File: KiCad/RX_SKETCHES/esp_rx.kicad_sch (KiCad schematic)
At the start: 5 parts, among them U2 ESP32-WROOM-32U

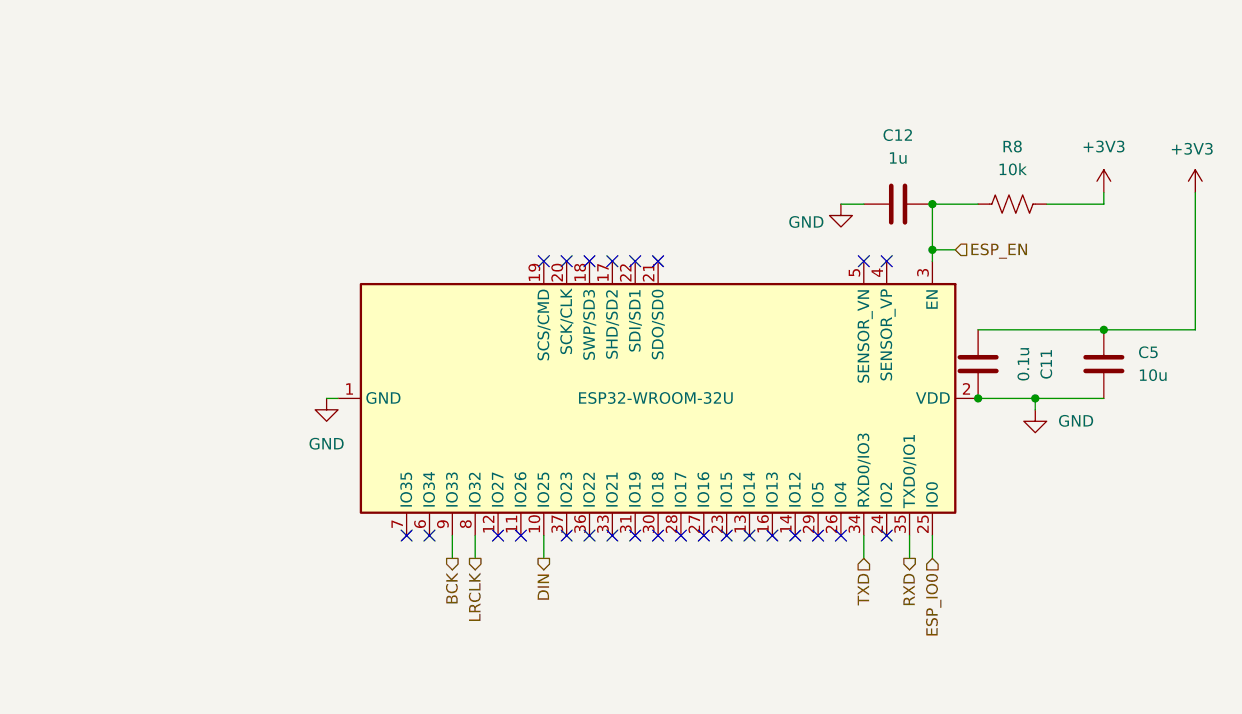
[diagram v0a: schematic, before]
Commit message: Rewire RX hierarchical labels and mark proto DNP parts.
Keep the rotated WROOM-32U and breadboard I2S GPIOs, but attach
ESP_EN/IO0, UART, and BCK/DIN/LRCLK to the pins that actually sit
there after the 270° rotate. Move PCM5102 I2S off FMT/DEMP/XSMT,
put amp shutdown on ~{SHDN}, keep the datasheet 470R+2.2nF filter,
DNP the experimental pot pad and MAX97220A input resistors, and
switch schematic passives to 0805 for hand assembly.

Co-authored-by: luciano <dlmuschamp@users.noreply.github.com>
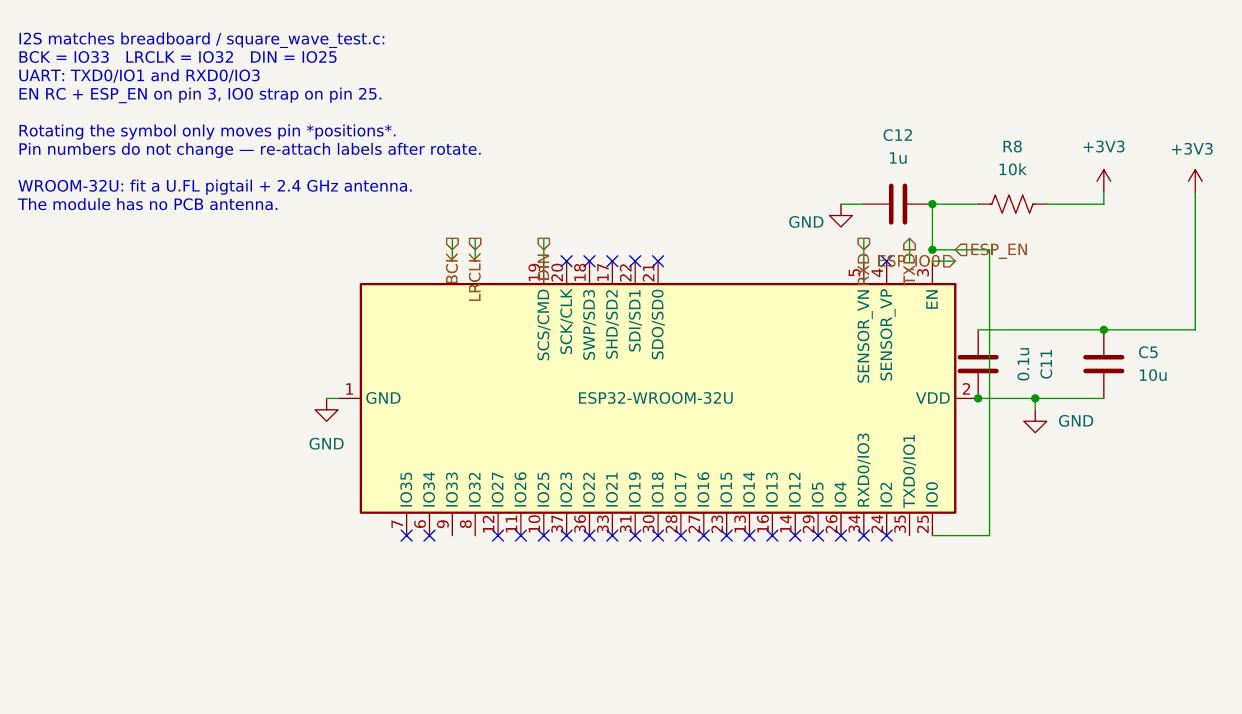
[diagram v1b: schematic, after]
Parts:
- C11, C12, C5: footprint Capacitor_SMD:C_0201_0603Metric -> Capacitor_SMD:C_0805_2012Metric
- R8: footprint Resistor_SMD:R_0201_0603Metric -> Resistor_SMD:R_0805_2012Metric
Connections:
- net BCK: no longer U2.9 (IO33)
- net DIN: now also U2.19 (SCS/CMD); no longer U2.10 (IO25)
- net ESP_EN: now also U2.25 (IO0); no longer U2.3 (EN)
- net ESP_IO0: now also U2.3 (EN); no longer U2.25 (IO0)
- net LRCLK: no longer U2.8 (IO32)
- net RXD: now also U2.5 (SENSOR_VN); no longer U2.35 (TXD0/IO1)
- net TXD: no longer U2.34 (RXD0/IO3)
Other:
- note added: "I2S matches breadboard / square_wave_test.c: BCK = IO33 LRCLK = IO32 DIN = IO25 UART: TXD0/IO1 and RXD0/IO3 EN RC + ESP_EN on pin 3, IO0 strap on pin 25. Rotating the symbol only moves pin *positions*. Pin numbers do not change — re-attach labels after rotate. WROOM-32U: fit a U.FL pigtail + 2.4 GHz antenna. The module has no PCB antenna."
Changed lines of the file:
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@@
 		(comment 3 "Will enter boot mode when communicating over UART. Functions normally otherwise.")
+	)
+	(text "I2S matches breadboard / square_wave_test.c:\nBCK = IO33   LRCLK = IO32   DIN = IO25\nUART: TXD0/IO1 and RXD0/IO3\nEN RC + ESP_EN on pin 3, IO0 strap on pin 25.\n\nRotating the symbol only moves pin *positions*.\nPin numbers do not change — re-attach labels after rotate.\n\nWROOM-32U: fit a U.FL pigtail + 2.4 GHz antenna.\nThe module has no PCB antenna."
+		(exclude_from_sim no)
+		(at 24.13 27.94 0)
+		(effects
+			(font
+				(size 1.27 1.27)
+			)
+			(justify left)
+		)
 	)
 	(junction
@@
 	)
 	(no_connect
-		(at 118.11 43.18)
+		(at 118.11 73.66)
 	)
 	(no_connect
@@
 	)
 	(no_connect
-		(at 82.55 43.18)
+		(at 82.55 73.66)
 	)
 	(no_connect
@@
 	(wire
 		(pts
-			(xy 118.11 73.66) (xy 118.11 76.2)
+			(xy 123.19 43.18) (xy 123.19 40.64)
 		)
 		(stroke
@@
 	(wire
 		(pts
-			(xy 72.39 73.66) (xy 72.39 76.2)
-		)
-		(stroke
-			(width 0)
-			(type default)
-		)
-	)
-	(wire
-		(pts
-			(xy 123.19 73.66) (xy 123.19 76.2)
+			(xy 72.39 43.18) (xy 72.39 40.64)
+		)
+		(stroke
+			(width 0)
+			(type default)
+		)
+	)
+	(wire
+		(pts
+			(xy 118.11 43.18) (xy 118.11 40.64)
 		)
 		(stroke
@@
 	(wire
 		(pts
-			(xy 74.93 76.2) (xy 74.93 73.66)
+			(xy 74.93 43.18) (xy 74.93 40.64)
 		)
 		(stroke
@@
 	(wire
 		(pts
-			(xy 82.55 73.66) (xy 82.55 76.2)
-		)
-		(stroke
-			(width 0)
-			(type default)
-		)
-	)
-	(wire
-		(pts
-			(xy 125.73 43.18) (xy 125.73 41.91)
+			(xy 82.55 43.18) (xy 82.55 40.64)
+		)
+		(stroke
+			(width 0)
+			(type default)
+		)
+	)
+	(wire
+		(pts
+			(xy 125.73 73.66) (xy 132.08 73.66)
+		)
+		(stroke
+			(width 0)
+			(type default)
+		)
+	)
+	(wire
+		(pts
+			(xy 132.08 73.66) (xy 132.08 41.91)
+		)
+		(stroke
+			(width 0)
+			(type default)
+		)
+	)
+	(wire
+		(pts
+			(xy 132.08 41.91) (xy 128.27 41.91)
 		)
 		(stroke
@@
 	(wire
 		(pts
-			(xy 125.73 73.66) (xy 125.73 76.2)
+			(xy 125.73 43.18) (xy 128.27 43.18)
 		)
 		(stroke
@@
 	(hierarchical_label "RXD"
 		(shape output)
-		(at 123.19 76.2 270)
+		(at 118.11 40.64 90)
 		(effects
 			(font
@@
 	(hierarchical_label "ESP_IO0"
 		(shape input)
-		(at 125.73 76.2 270)
+		(at 128.27 43.18 0)
 		(effects
 			(font
@@
 	(hierarchical_label "LRCLK"
 		(shape output)
-		(at 74.93 76.2 270)
+		(at 74.93 40.64 90)
 		(effects
 			(font
@@
 	(hierarchical_label "BCK"
 		(shape output)
-		(at 72.39 76.2 270)
+		(at 72.39 40.64 90)
 		(effects
 			(font
@@
 	(hierarchical_label "DIN"
 		(shape output)
-		(at 82.55 76.2 270)
+		(at 82.55 40.64 90)
 		(effects
 			(font
@@
 	(hierarchical_label "TXD"
 		(shape input)
-		(at 118.11 76.2 270)
+		(at 123.19 40.64 90)
 		(effects
 			(font
@@
 			)
 		)
-		(property "Footprint" "Capacitor_SMD:C_0201_0603Metric"
+		(property "Footprint" "Capacitor_SMD:C_0805_2012Metric"
 			(at 145.7452 58.42 0)
 			(hide yes)
@@
 			)
 		)
-		(property "Footprint" "Resistor_SMD:R_0201_0603Metric"
+		(property "Footprint" "Resistor_SMD:R_0805_2012Metric"
 			(at 134.366 37.846 90)
 			(hide yes)
@@
 			)
 		)
-		(property "Footprint" "Capacitor_SMD:C_0201_0603Metric"
+		(property "Footprint" "Capacitor_SMD:C_0805_2012Metric"
 			(at 125.73 35.8648 0)
 			(hide yes)
@@
 			)
 		)
-		(property "Footprint" "Capacitor_SMD:C_0201_0603Metric"
+		(property "Footprint" "Capacitor_SMD:C_0805_2012Metric"
 			(at 131.7752 58.42 0)
 			(hide yes)

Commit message: Document the RX transfer and add ANT1 on the ESP sheet.
Rewrite the README for no display, matching 10,000 mAh USB-C banks
on TX and RX, the firmware I2S map, and first-board KiCad pitfalls.
Place ANT1 as a BOM-only 2.4 GHz U.FL pigtail that mates to the
WROOM-32U module connector (no GPIO, no PCB antenna footprint).

Co-authored-by: luciano <dlmuschamp@users.noreply.github.com>
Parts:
- added ANT1: 2.4GHz_U.FL_pigtail, symbol Device:Antenna
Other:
- note added: "I2S matches breadboard / square_wave_test.c: BCK = IO33 LRCLK = IO32 DIN = IO25 UART: TXD0/IO1 and RXD0/IO3 EN RC + ESP_EN on pin 3, IO0 strap on pin 25. Rotating the symbol only moves pin *positions*. Pin numbers do not change — re-attach labels after rotate. ANT1 = 2.4 GHz U.FL/IPEX pigtail (BOM only). Mates to the 32U on-module U.FL. No GPIO, no PCB antenna."
- note removed: "I2S matches breadboard / square_wave_test.c: BCK = IO33 LRCLK = IO32 DIN = IO25 UART: TXD0/IO1 and RXD0/IO3 EN RC + ESP_EN on pin 3, IO0 strap on pin 25. Rotating the symbol only moves pin *positions*. Pin numbers do not change — re-attach labels after rotate. WROOM-32U: fit a U.FL pigtail + 2.4 GHz antenna. The module has no PCB antenna."
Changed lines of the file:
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@@
 		(comment 3 "Will enter boot mode when communicating over UART. Functions normally otherwise.")
 	)
-	(text "I2S matches breadboard / square_wave_test.c:\nBCK = IO33   LRCLK = IO32   DIN = IO25\nUART: TXD0/IO1 and RXD0/IO3\nEN RC + ESP_EN on pin 3, IO0 strap on pin 25.\n\nRotating the symbol only moves pin *positions*.\nPin numbers do not change — re-attach labels after rotate.\n\nWROOM-32U: fit a U.FL pigtail + 2.4 GHz antenna.\nThe module has no PCB antenna."
+	(text "I2S matches breadboard / square_wave_test.c:\nBCK = IO33   LRCLK = IO32   DIN = IO25\nUART: TXD0/IO1 and RXD0/IO3\nEN RC + ESP_EN on pin 3, IO0 strap on pin 25.\n\nRotating the symbol only moves pin *positions*.\nPin numbers do not change — re-attach labels after rotate.\n\nANT1 = 2.4 GHz U.FL/IPEX pigtail (BOM only).\nMates to the 32U on-module U.FL. No GPIO, no PCB antenna."
 		(exclude_from_sim no)
 		(at 24.13 27.94 0)
@@
 					(unit 1)
 				)
+			)
+		)
+	)
+	(symbol
+		(lib_id "Device:Antenna")
+		(at 36.83 88.9 0)
+		(unit 1)
+		(body_style 1)
+		(exclude_from_sim yes)
+		(in_bom yes)
+		(on_board no)
+		(in_pos_files no)
+		(dnp no)
+		(property "Reference" "ANT1"
+			(at 36.83 82.55 0)
+			(show_name no)
+			(do_not_autoplace no)
+			(effects
+				(font
+					(size 1.27 1.27)
+				)
+			)
+		)
+		(property "Value" "2.4GHz_U.FL_pigtail"
+			(at 41.91 88.9 0)
+			(show_name no)
+			(do_not_autoplace no)
+			(effects
+				(font
+					(size 1.27 1.27)
+				)
+				(justify left)
+			)
+		)
+		(property "Footprint" ""
+			(at 36.83 88.9 0)
+			(hide yes)
+			(show_name no)
+			(do_not_autoplace no)
+			(effects
+				(font
+					(size 1.27 1.27)
+				)
+			)
+		)
+		(property "Datasheet" ""
+			(at 36.83 88.9 0)
+			(hide yes)
+			(show_name no)
+			(do_not_autoplace no)
+			(effects
+				(font
+					(size 1.27 1.27)
+				)
+			)
+		)
+		(property "Description" "2.4 GHz 50 ohm antenna on U.FL/IPEX pigtail. Mates to WROOM-32U module U.FL. Not a GPIO."
+			(at 36.83 88.9 0)
+			(hide yes)
+			(show_name no)
+			(do_not_autoplace no)
+			(effects
+				(font
+					(size 1.27 1.27)
+				)
+			)
+		)
+		(instances
+			(project "ESP_32_IEM_RIG_RX_VER_1.0"
+				(path "/98787dcf-424f-4647-bb79-9127f0f74bda/12633c0c-fb68-4c25-af81-bead6c15ab98"
+					(reference "ANT1")
+					(unit 1)
+				)

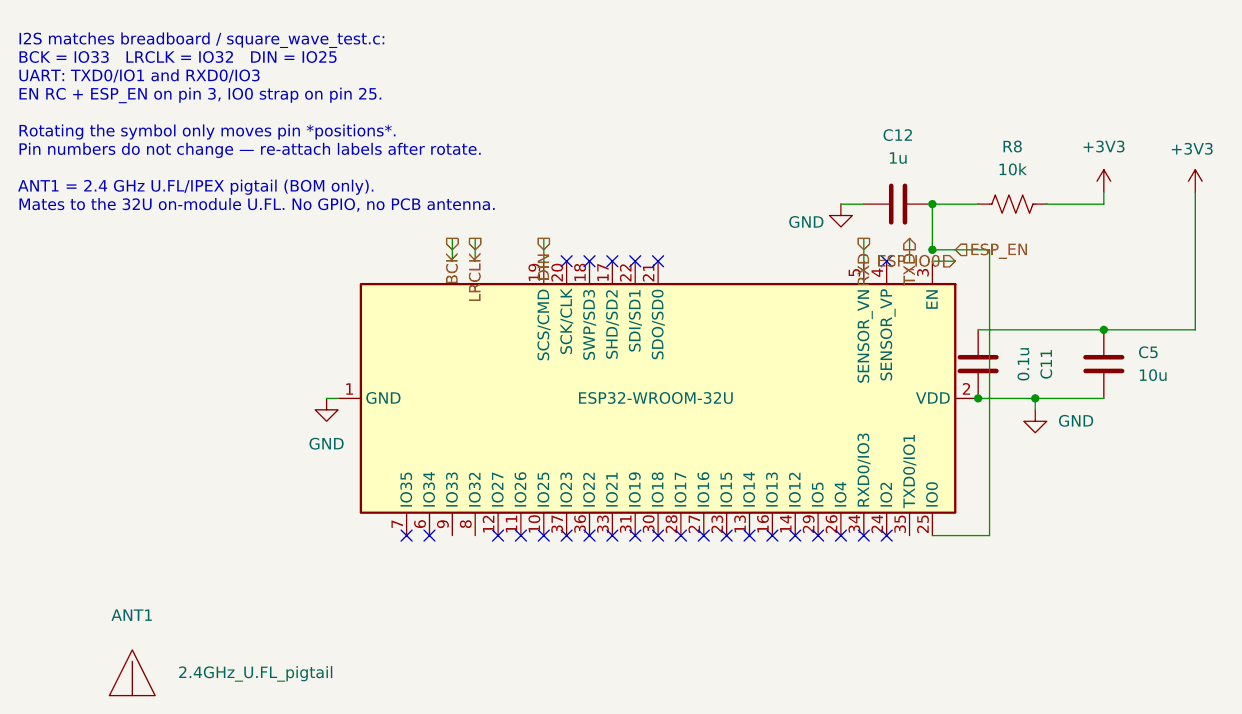
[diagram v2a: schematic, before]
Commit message: Align RX passives and analog nets with the part datasheets.
Put every R/C on the 0805 HandSolder footprint. Rewire the PCM5102
470R filter onto OUTL/OUTR, decouple LDOO, and land the flying cap
on CAPP/CAPM. Move the headphone jack off PVSS/SVSS onto OUTL/OUTR
with a PVSS hold cap. Tie CP2102C VIO to VDD, pull RST up, add the
LM3940 0.47uF Cin, and pull IO0 up for normal boot.

Co-authored-by: luciano <dlmuschamp@users.noreply.github.com>
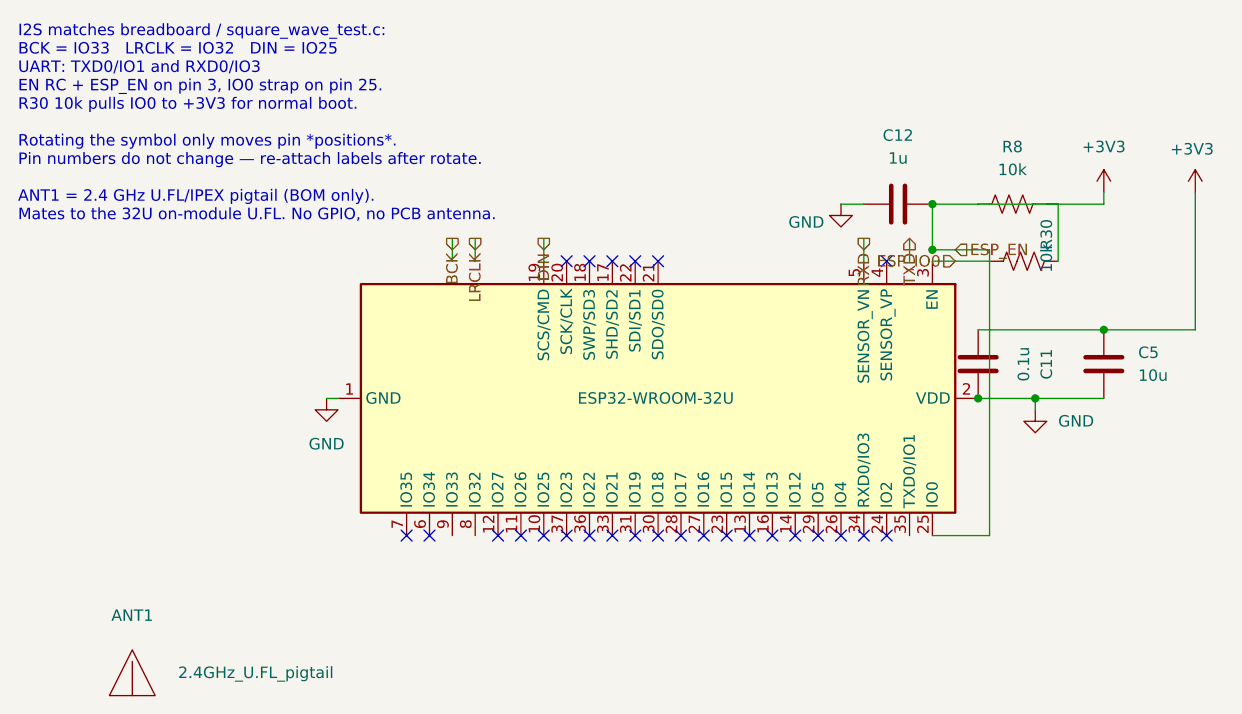
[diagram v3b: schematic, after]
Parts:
- added R30: 10k, Resistor_SMD:R_0805_2012Metric_Pad1.20x1.40mm_HandSolder, symbol Device:R_US
- C11, C12, C5: footprint Capacitor_SMD:C_0805_2012Metric -> Capacitor_SMD:C_0805_2012Metric_Pad1.15x1.40mm_HandSolder
- R8: footprint Resistor_SMD:R_0805_2012Metric -> Resistor_SMD:R_0805_2012Metric_Pad1.20x1.40mm_HandSolder
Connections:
- net ESP_EN is gone; now on net +3V3: C12.2, R8.2, U2.25 (IO0)
- net +3V3: now also R30.2
- net ESP_IO0: now also R30.1
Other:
- note added: "I2S matches breadboard / square_wave_test.c: BCK = IO33 LRCLK = IO32 DIN = IO25 UART: TXD0/IO1 and RXD0/IO3 EN RC + ESP_EN on pin 3, IO0 strap on pin 25. R30 10k pulls IO0 to +3V3 for normal boot. Rotating the symbol only moves pin *positions*. Pin numbers do not change — re-attach labels after rotate. ANT1 = 2.4 GHz U.FL/IPEX pigtail (BOM only). Mates to the 32U on-module U.FL. No GPIO, no PCB a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"
- note removed: "I2S matches breadboard / square_wave_test.c: BCK = IO33 LRCLK = IO32 DIN = IO25 UART: TXD0/IO1 and RXD0/IO3 EN RC + ESP_EN on pin 3, IO0 strap on pin 25. Rotating the symbol only moves pin *positions*. Pin numbers do not change — re-attach labels after rotate. ANT1 = 2.4 GHz U.FL/IPEX pigtail (BOM only). Mates to the 32U on-module U.FL. No GPIO, no PCB antenna."
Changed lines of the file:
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@@
 		(comment 3 "Will enter boot mode when communicating over UART. Functions normally otherwise.")
 	)
-	(text "I2S matches breadboard / square_wave_test.c:\nBCK = IO33   LRCLK = IO32   DIN = IO25\nUART: TXD0/IO1 and RXD0/IO3\nEN RC + ESP_EN on pin 3, IO0 strap on pin 25.\n\nRotating the symbol only moves pin *positions*.\nPin numbers do not change — re-attach labels after rotate.\n\nANT1 = 2.4 GHz U.FL/IPEX pigtail (BOM only).\nMates to the 32U on-module U.FL. No GPIO, no PCB antenna."
+	(wire
+		(pts
+			(xy 128.27 43.18) (xy 132.08 43.18)
+		)
+		(stroke
+			(width 0)
+			(type default)
+		)
+	)
+	(wire
+		(pts
+			(xy 139.7 43.18) (xy 139.7 36.83)
+		)
+		(stroke
+			(width 0)
+			(type default)
+		)
+	)
+	(wire
+		(pts
+			(xy 139.7 36.83) (xy 130.81 36.83)
+		)
+		(stroke
+			(width 0)
+			(type default)
+		)
+	)
+	(symbol
+		(lib_id "Device:R_US")
+		(at 135.89 43.18 90)
+		(unit 1)
+		(body_style 1)
+		(exclude_from_sim no)
+		(in_bom yes)
+		(on_board yes)
+		(in_pos_files yes)
+		(dnp no)
+		(property "Reference" "R30"
+			(at 138.42999999999998 41.91 0)
+			(show_name no)
+			(do_not_autoplace no)
+			(effects
+				(font
+					(size 1.27 1.27)
+				)
+				(justify left)
+			)
+		)
+		(property "Value" "10k"
+			(at 138.42999999999998 44.45 0)
+			(show_name no)
+			(do_not_autoplace no)
+			(effects
+				(font
+					(size 1.27 1.27)
+				)
+				(justify left)
+			)
+		)
+		(property "Footprint" "Resistor_SMD:R_0805_2012Metric_Pad1.20x1.40mm_HandSolder"
+			(at 135.89 43.18 0)
+			(hide yes)
+			(show_name no)
+			(do_not_autoplace no)
+			(effects
+				(font
+					(size 1.27 1.27)
+				)
+			)
+		)
+		(property "Datasheet" ""
+			(at 135.89 43.18 0)
+			(hide yes)
+			(show_name no)
+			(do_not_autoplace no)
+			(effects
+				(font
+					(size 1.27 1.27)
+				)
+			)
+		)
+		(property "Description" "Resistor, US symbol"
+			(at 135.89 43.18 0)
+			(hide yes)
+			(show_name no)
+			(do_not_autoplace no)
+			(effects
+				(font
+					(size 1.27 1.27)
+				)
+			)
+		)
+		(pin "2"
+		)
+		(pin "1"
+		)
+		(instances
+			(project "ESP_32_IEM_RIG_RX_VER_1.0"
+				(path "/98787dcf-424f-4647-bb79-9127f0f74bda/12633c0c-fb68-4c25-af81-bead6c15ab98"
+					(reference "R30")
+					(unit 1)
+				)
+			)
+		)
+	)
+	(text "I2S matches breadboard / square_wave_test.c:\nBCK = IO33   LRCLK = IO32   DIN = IO25\nUART: TXD0/IO1 and RXD0/IO3\nEN RC + ESP_EN on pin 3, IO0 strap on pin 25.\nR30 10k pulls IO0 to +3V3 for normal boot.\n\nRotating the symbol only moves pin *positions*.\nPin numbers do not change — re-attach labels after rotate.\n\nANT1 = 2.4 GHz U.FL/IPEX pigtail (BOM only).\nMates to the 32U on-module U.FL. No GPIO, no PCB antenna."
 		(exclude_from_sim no)
 		(at 24.13 27.94 0)
@@
 			)
 		)
-		(property "Footprint" "Capacitor_SMD:C_0805_2012Metric"
+		(property "Footprint" "Capacitor_SMD:C_0805_2012Metric_Pad1.15x1.40mm_HandSolder"
 			(at 145.7452 58.42 0)
 			(hide yes)
@@
 	)
 	(symbol
-		(lib_id "power:+3.3V")
+		(lib_id "power:+3V3")
 		(at 154.94 35.56 0)
 		(unit 1)
@@
 			)
 		)
-		(property "Footprint" "Resistor_SMD:R_0805_2012Metric"
+		(property "Footprint" "Resistor_SMD:R_0805_2012Metric_Pad1.20x1.40mm_HandSolder"
 			(at 134.366 37.846 90)
 			(hide yes)
@@
 			)
 		)
-		(property "Footprint" "Capacitor_SMD:C_0805_2012Metric"
+		(property "Footprint" "Capacitor_SMD:C_0805_2012Metric_Pad1.15x1.40mm_HandSolder"
 			(at 125.73 35.8648 0)
 			(hide yes)
@@
 			)
 		)
-		(property "Footprint" "Capacitor_SMD:C_0805_2012Metric"
+		(property "Footprint" "Capacitor_SMD:C_0805_2012Metric_Pad1.15x1.40mm_HandSolder"
 			(at 131.7752 58.42 0)
 			(hide yes)
